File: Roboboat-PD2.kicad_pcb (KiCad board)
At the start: 2 copper layers, 78 x 60.7 mm, 52 parts, among them J1 14.4V, J10 Motor, J11 Motor, J12 Motor, J13 Motor, J14 Motor, J15 Motor, J16 Motor, J17 GND TP, J18 PGOOD TP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

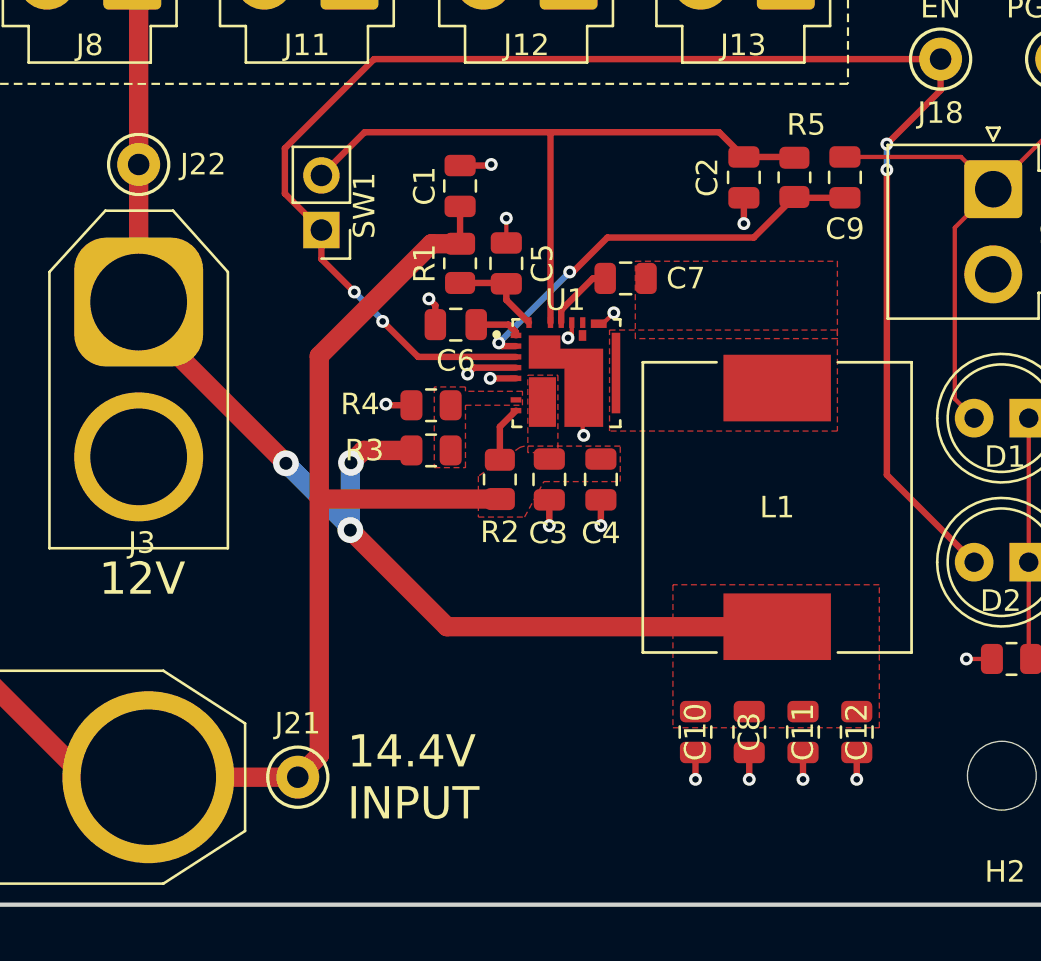
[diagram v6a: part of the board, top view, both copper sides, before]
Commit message: add thermal pours
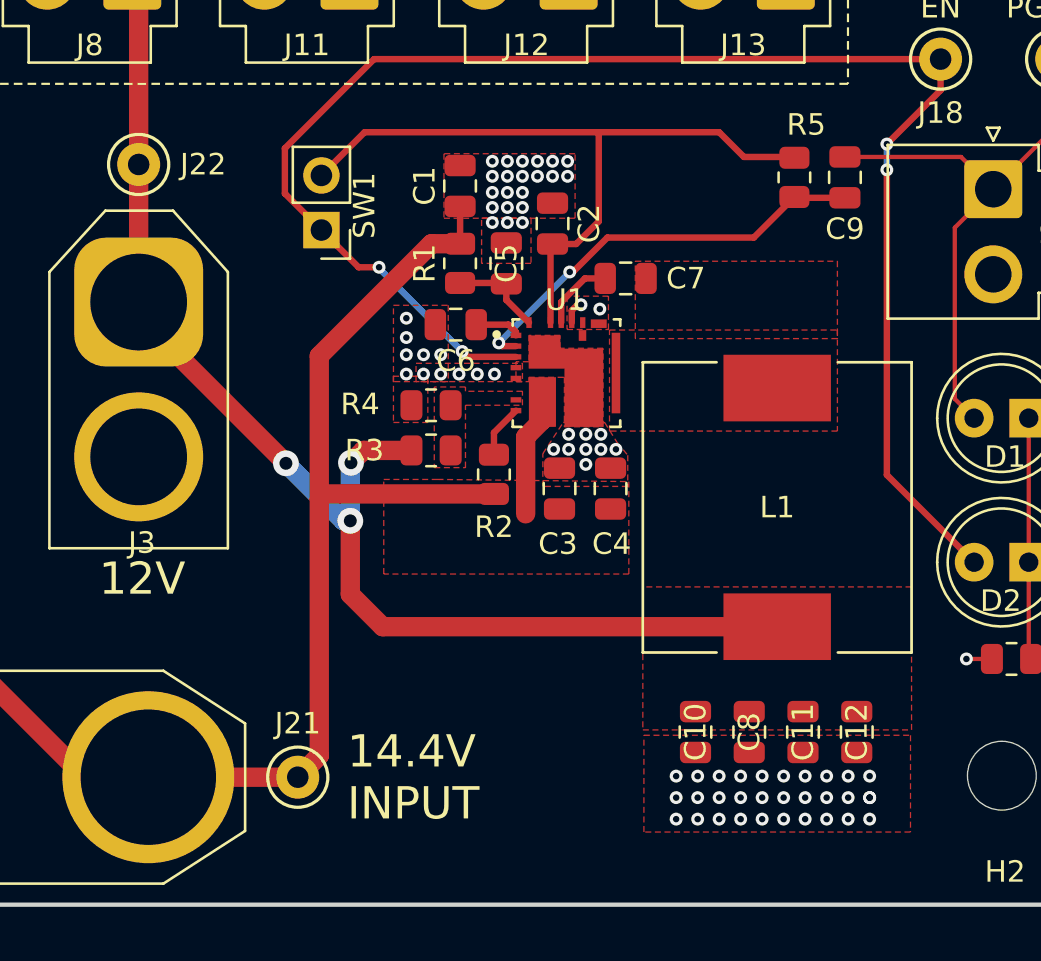
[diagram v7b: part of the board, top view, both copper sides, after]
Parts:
- moved C2 9.16 mm to (145.8, 97.3), turned to 90 degrees
- moved C3 0.64 mm to (146.1, 109.6), turned to 90 degrees
- moved C4 0.62 mm to (148.4, 109.6), turned to 90 degrees
- moved R2 0.36 mm to (143.0, 109.0)
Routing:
- net GND: track 22.3 -> 2.29 mm, vias 17 -> 75
- net +14.4V: track 89.7 -> 94.7 mm
- net /VCC: track 32.2 -> 33.6 mm
- net /EN: track 75.2 -> 74.4 mm
- added copper zone on F.Cu, net GND

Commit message: add thermal vias
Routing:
- net +14.4V: vias 0 -> 34
- net +12V: vias 3 -> 33
